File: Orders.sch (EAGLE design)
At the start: 5 parts, among them J1 10104111-0001LF

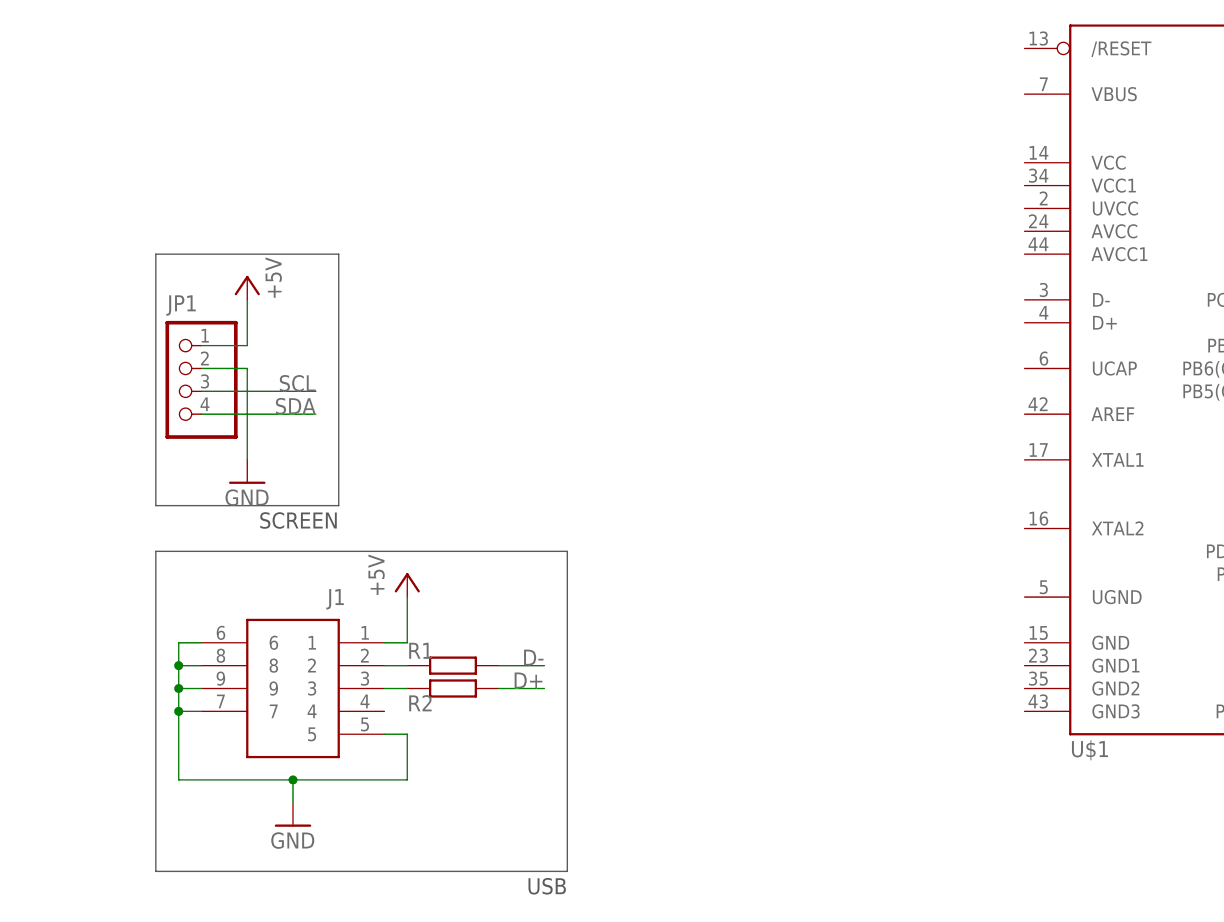
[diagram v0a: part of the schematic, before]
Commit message: Added I2C pull-up resistances
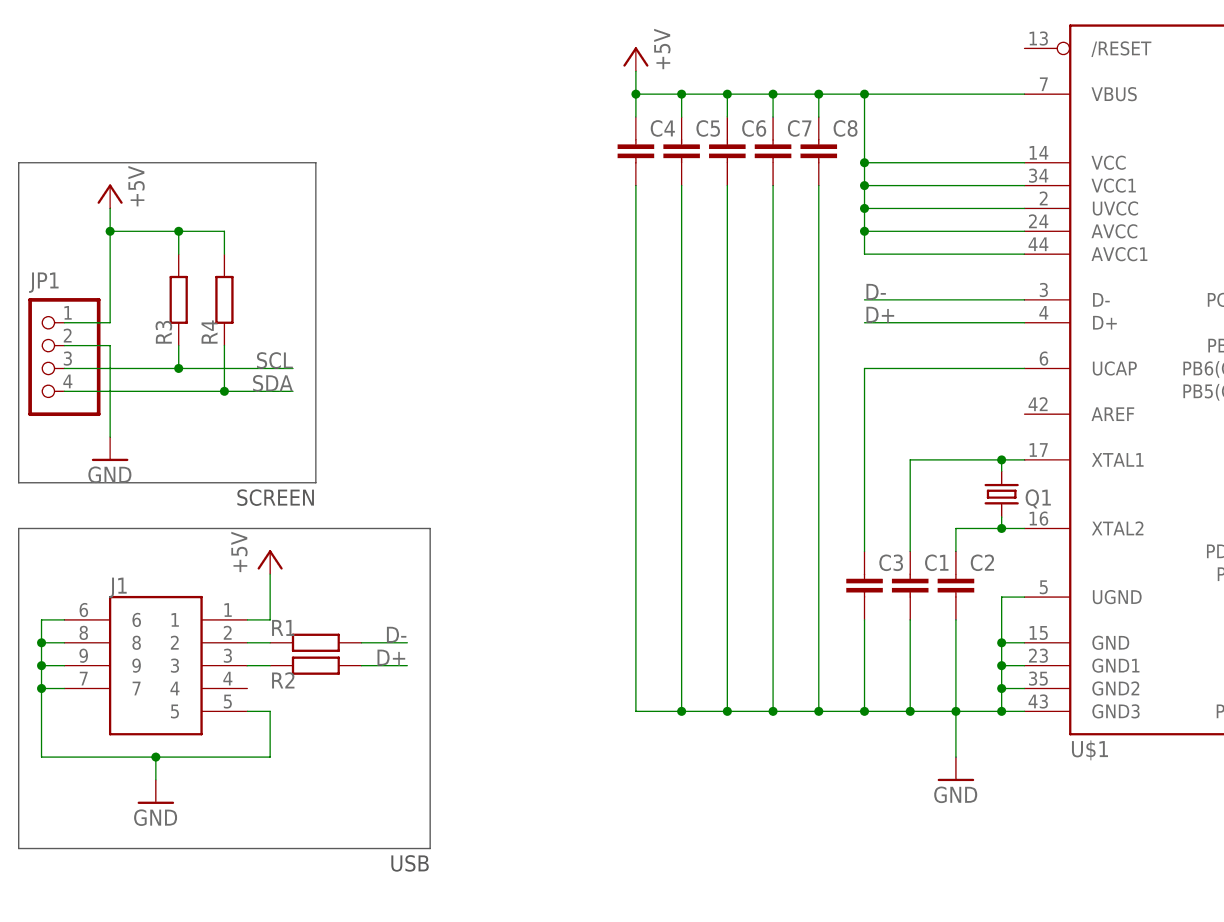
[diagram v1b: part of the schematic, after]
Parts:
- added C1, C2, C3, C4, C5, C6, C7, C8: (no value), rcl:C-EUC1206
- added Q1: (no value), adafruit:CRYSTALHC49UP
- added R3, R4: (no value), rcl:R-EU_R1206
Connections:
- new net N$3: C1.1, Q1.2, U$1.XTAL1
- new net N$4: C2.1, Q1.1, U$1.XTAL2
- new net N$5: C3.1, U$1.UCAP
- net +5V: now also C4.1, C5.1, C6.1, C7.1, C8.1, R3.2, R4.2, U$1.AVCC, U$1.AVCC1, U$1.UVCC, U$1.VBUS, U$1.VCC, U$1.VCC1
- net D+: now also U$1.D+
- net D-: now also U$1.D-
- net GND: now also C1.2, C2.2, C3.2, C4.2, C5.2, C6.2, C7.2, C8.2, U$1.GND, U$1.GND1, U$1.GND2, U$1.GND3, U$1.UGND
- net SCL: now also R3.1
- net SDA: now also R4.1
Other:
- moved on the sheet: J1, JP1, R1, R2

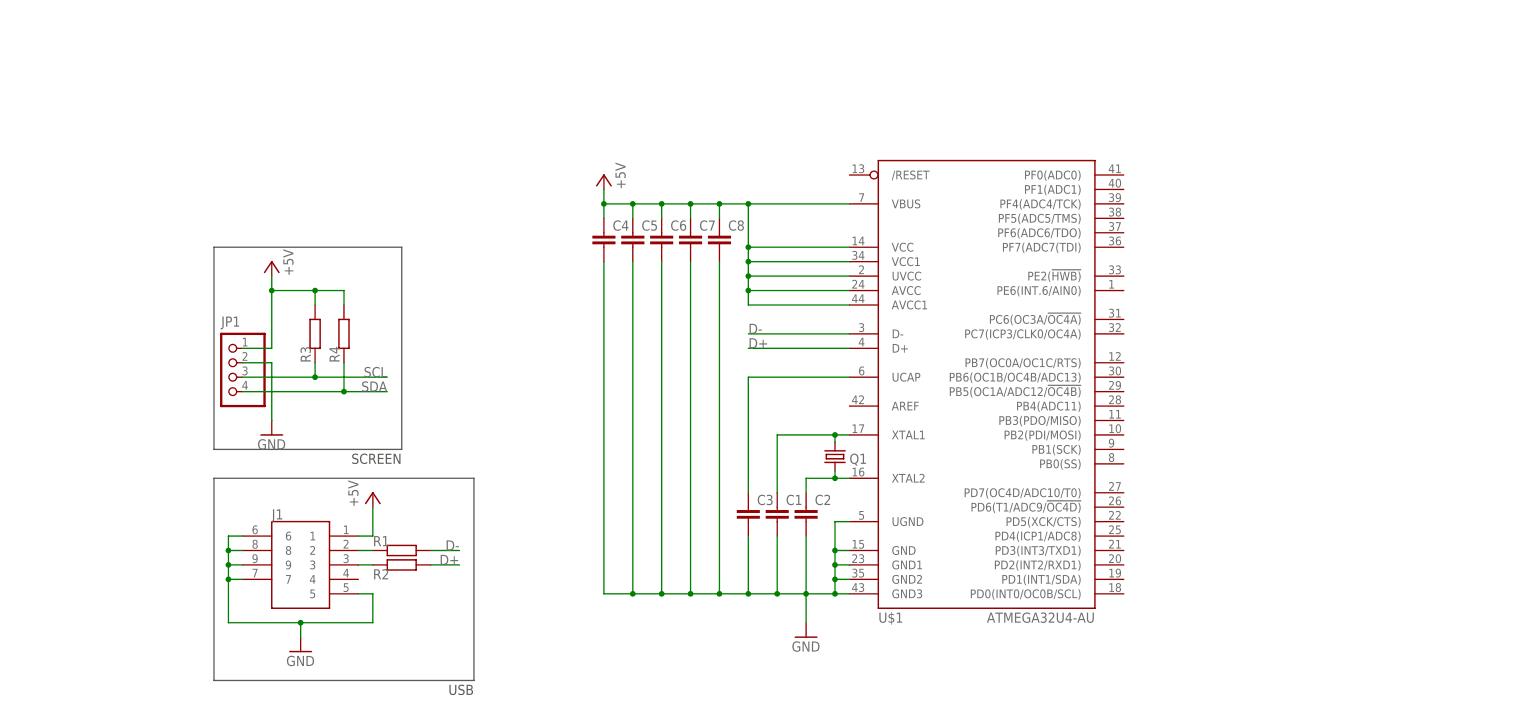
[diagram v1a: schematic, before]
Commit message: Added passives for uC
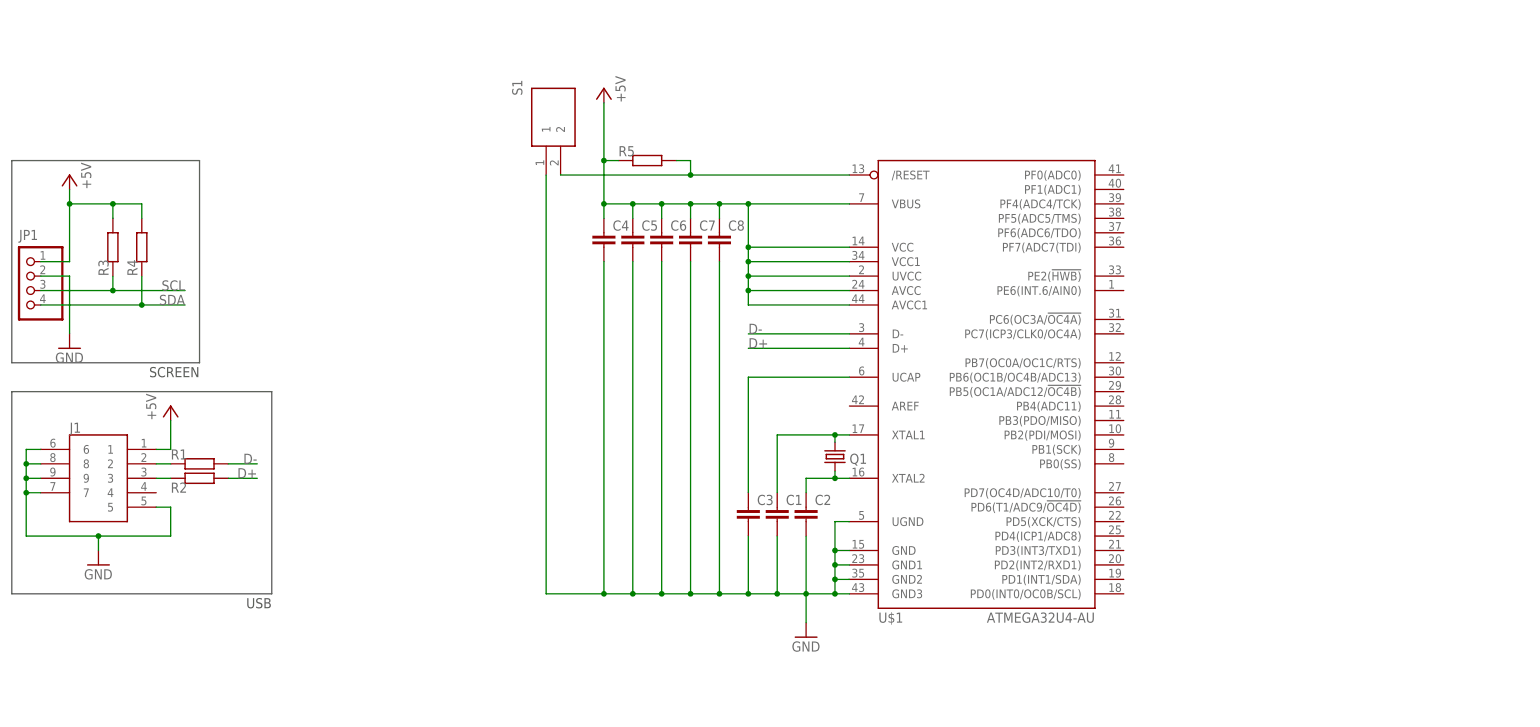
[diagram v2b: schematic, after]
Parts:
- added R5: (no value), rcl:R-EU_R1206
- added S1: KSR231GLFS, Switch:KSR231GLFS
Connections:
- new net N$6: R5.2, S1.2, U$1./RESET
- net +5V: now also R5.1
- net GND: now also S1.1
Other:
- moved on the sheet: J1, JP1, R1, R2, R3, R4

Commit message: Finished schematic
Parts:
- added JP2: (no value), pinhead:PINHD-1X6
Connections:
- new net RX: JP2.4, U$1.PD2(INT2/RXD1)
- new net TX: JP2.5, U$1.PD3(INT3/TXD1)
- net +5V: now also JP2.2
- net GND: now also JP2.3
- net SCL: now also U$1.PD0(INT0/OC0B/SCL)
- net SDA: now also U$1.PD1(INT1/SDA)
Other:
- note added: "BLUETOOTH"
- moved on the sheet: C1, C2, C3, C4, C5, C6, C7, C8, J1, JP1, Q1, R1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

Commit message: Refined ground planes
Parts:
- added J_SPI: (no value), pinhead:PINHD-2X3
- added LED1, LED2, PWR: (no value), led:LED3MM
- added R10, R11, R6, R7, R8, R9: (no value), rcl:R-EU_R1206
- added S2, S3, S4: KSR231GLFS, Switch:KSR231GLFS
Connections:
- net N$5 renamed UCAP
- new net L1: R10.2, U$1.PB7(OC0A/OC1C/RTS)
- new net L2: R11.2, U$1.PB0(SS)
- new net MISO: J_SPI.1, U$1.PB3(PDO/MISO)
- new net MOSI: J_SPI.4, U$1.PB2(PDI/MOSI)
- new net N$5: PWR.A, R9.1
- new net N$7: LED2.A, R11.1
- new net RST: J_SPI.5, R5.2, S1.1, U$1./RESET
- new net SCK: J_SPI.3, U$1.PB1(SCK)
- new net TACT_1: R6.1, S2.1, U$1.PF4(ADC4/TCK)
- new net TACT_2: R7.1, S3.1, U$1.PF1(ADC1)
- new net TACT_3: R8.1, S4.1, U$1.PF0(ADC0)
- net +5V: now also J_SPI.2, R6.2, R7.2, R8.2, R9.2
- net GND: now also J_SPI.6, LED1.C, LED2.C, PWR.C, S1.2, S2.2, S3.2, S4.2; no longer S1.1
- net N$6: now also LED1.A, R10.1; no longer R5.2, S1.2, U$1./RESET
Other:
- note added: "LEDs"
- note added: "SPI"
- note added: "SWITCHES"
- moved on the sheet: J1, JP1, JP2, R1, R2, R3, R4

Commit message: Final commit, added software
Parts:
- renumbered S1 to RST, S2 to UP, S3 to OK, S4 to DOWN, U$1 to U1
